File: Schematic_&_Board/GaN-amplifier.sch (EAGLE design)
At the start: 23 parts, among them T1 FDC3535, T2 NPN_MMBTA06FSCT, U1 TPS7A30XX, X1 SMA-142-0701-801/806, X2 SMA-142-0701-801/806

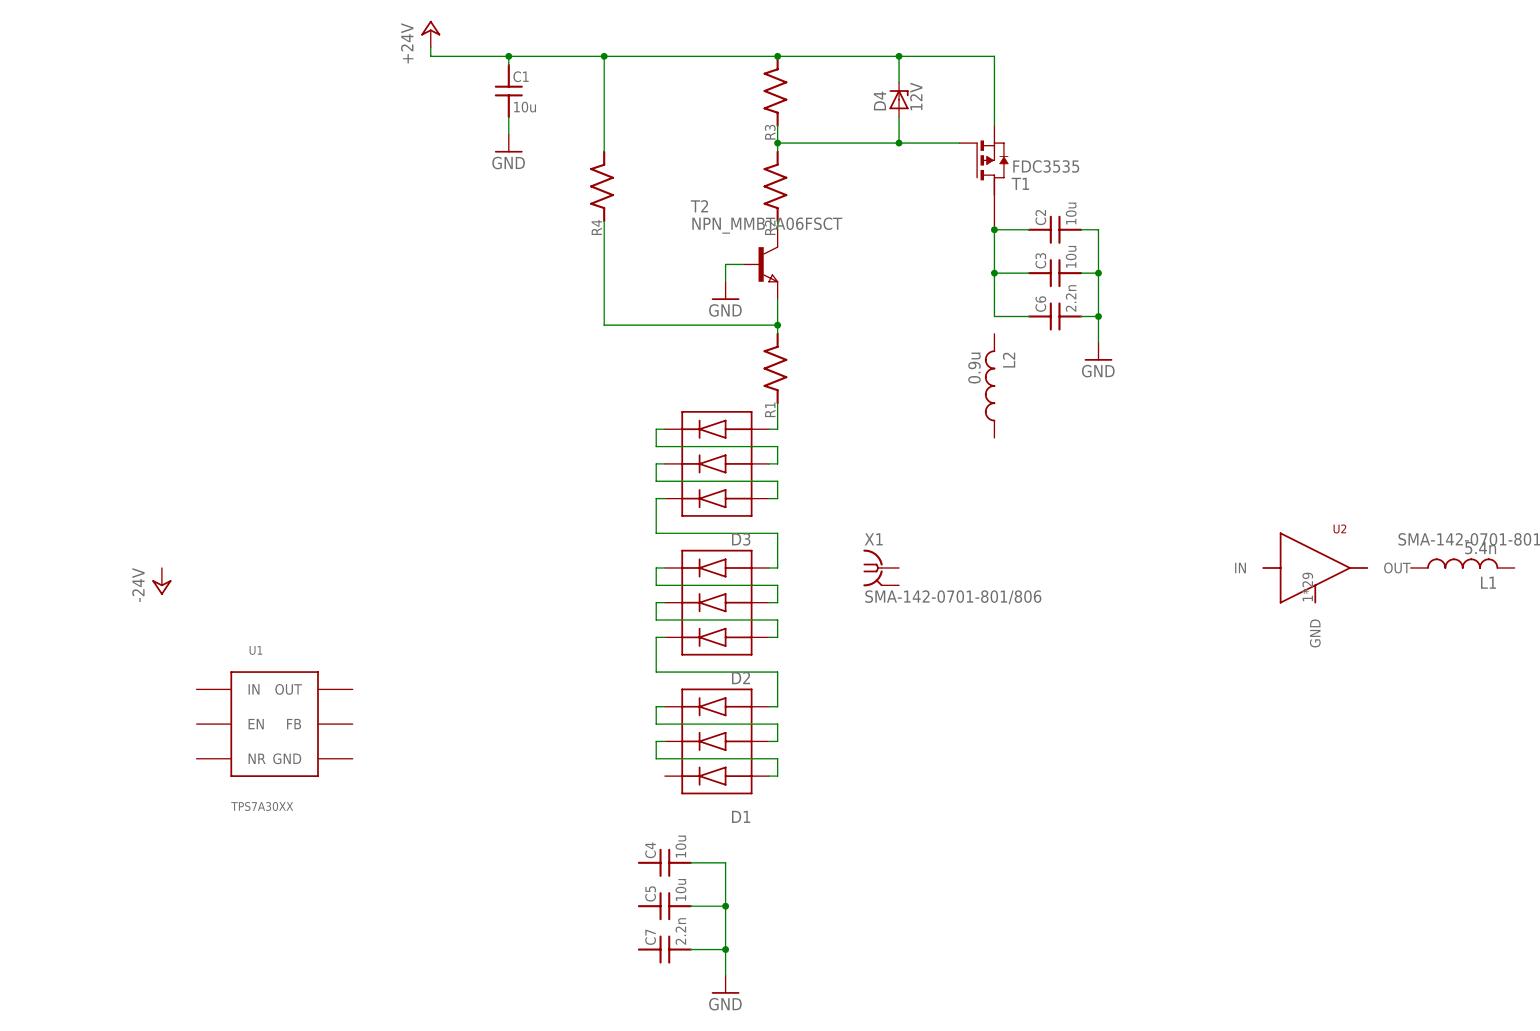
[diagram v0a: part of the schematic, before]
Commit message: Mostly designed power sequencing
This will all almost certainly be trashed, but it's a start.

DSB
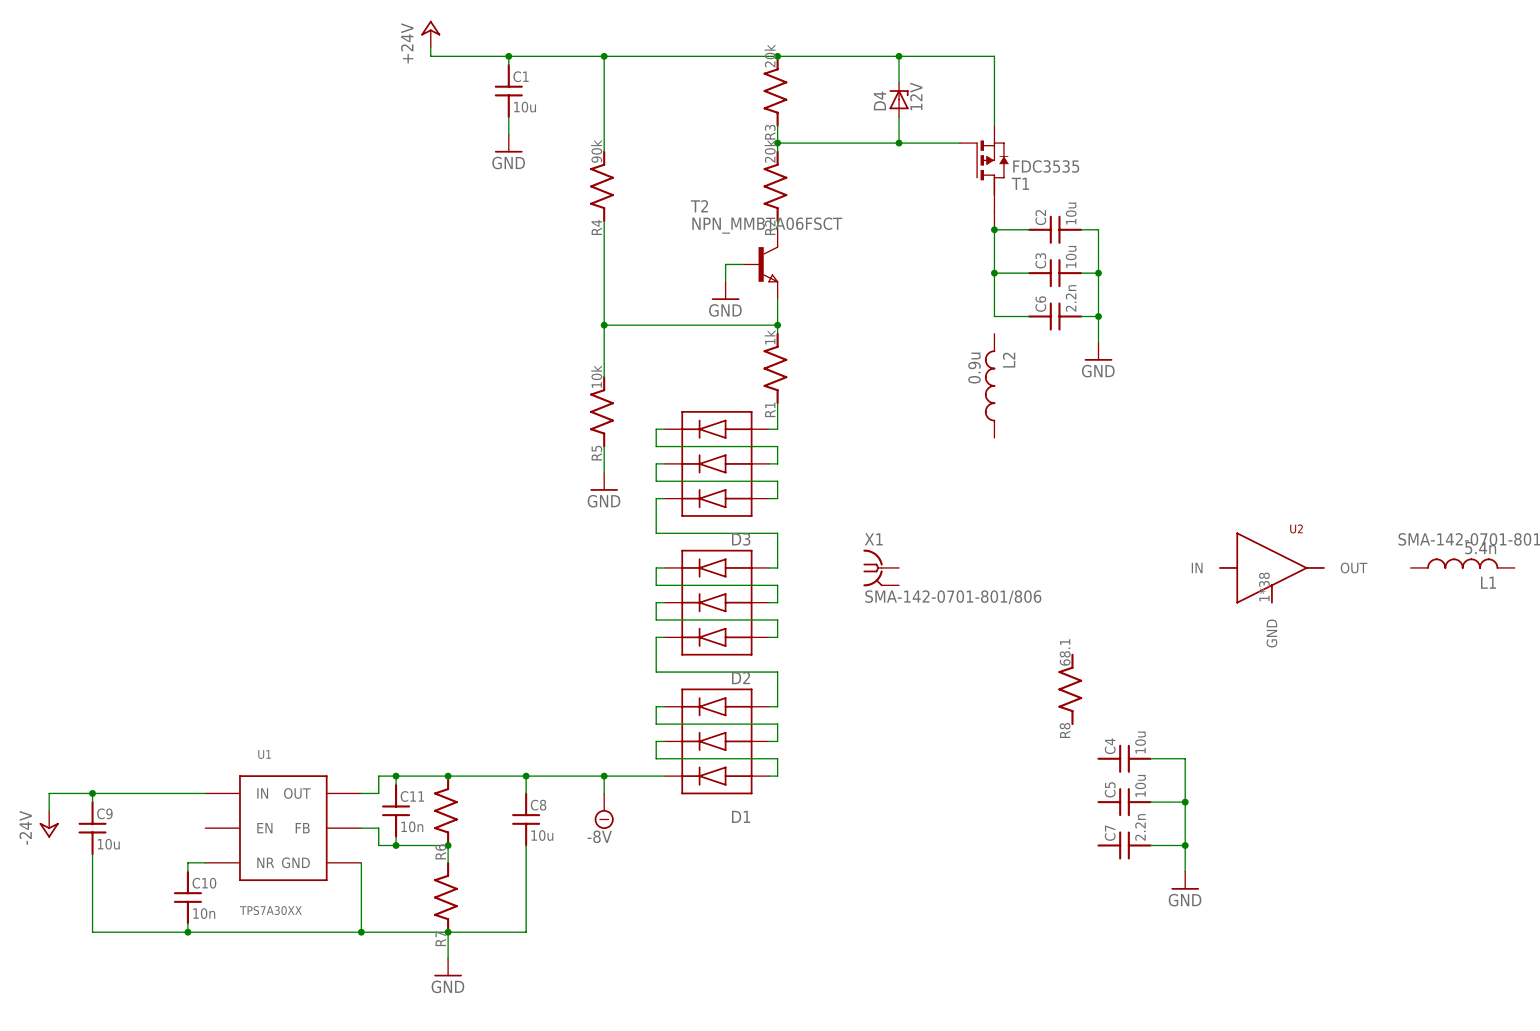
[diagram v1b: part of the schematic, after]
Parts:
- added C10, C11: 10n, jqi_passives:C_MLCC_SMDCMLCC_0402
- added C8, C9: 10u, jqi_passives:C_MLCC_SMDCMLCC_1206
- added R5: 10k, jqi_passives:R_SMDR0603
- added R6, R7: (no value), jqi_passives:R_SMDR0402
- added R8: 68.1, jqi_passives:R_SMDR0603
- R1: value (none) -> 1k
- R2, R3: value (none) -> 20k
- R4: value (none) -> 90k
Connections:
- new net -24V: C9.1, U1.IN
- new net -8V: C11.1, C8.1, D1.C1, R6.2, U1.OUT
- new net N$15: C11.2, R6.1, R7.2, U1.FB
- new net N$17: C10.1, U1.NR
- net GND: now also C10.2, C8.2, C9.2, R5.1, R7.1, U1.GND
- net N$3: now also R5.2
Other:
- moved on the sheet: C4, C5, C7, U1, U2

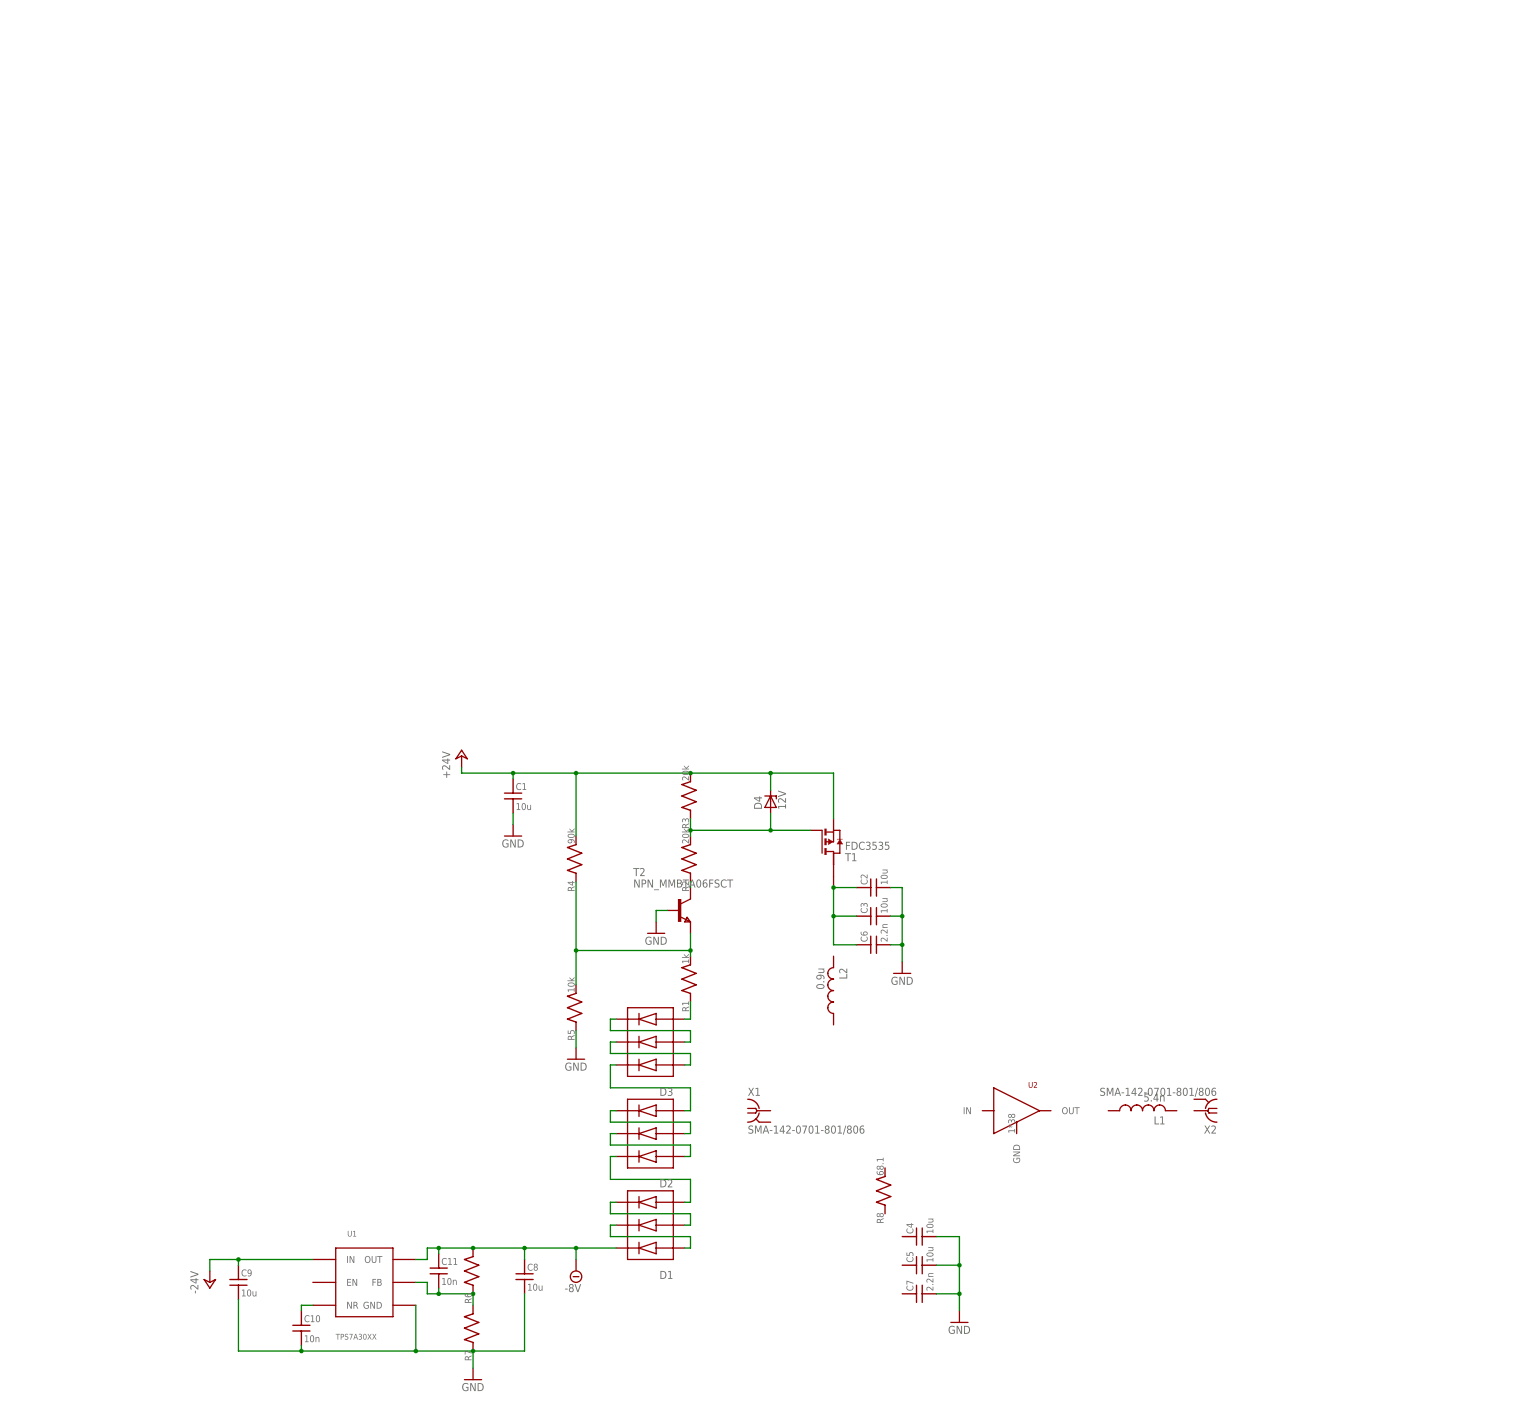
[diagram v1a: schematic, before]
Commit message: Change power sequencing
Switched to using LTC2924 for power sequencing.

DSB
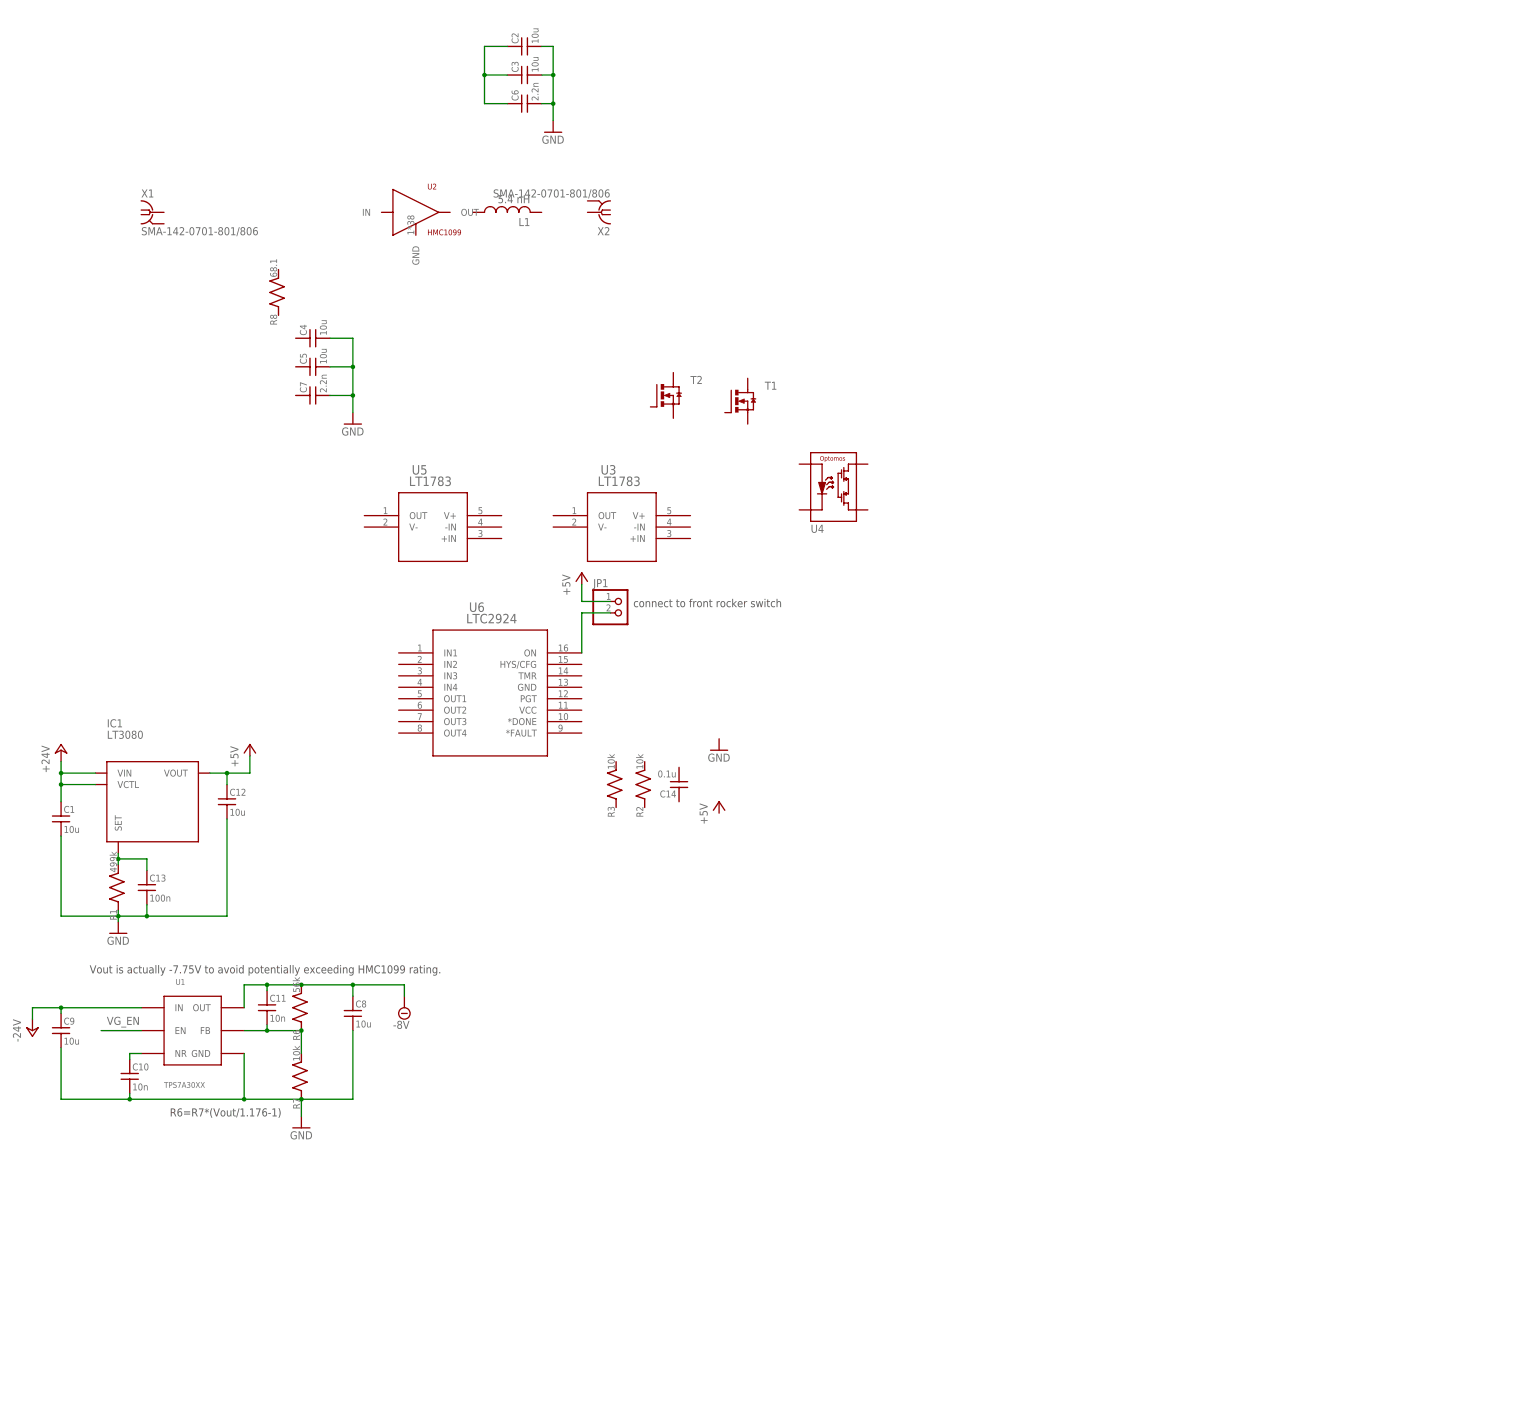
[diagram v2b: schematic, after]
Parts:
- removed D1, D2, D3: BAS16TW, qkdlab_alessandro:BAS16TW
- removed D4: 12V, qkdlab_alessandro:ZENER-DIODE
- removed L2: 0.9u, coilcraft-jqi:1008AF-XX
- removed R4: 90k, jqi_passives:R_SMDR0603
- removed R5: 10k, jqi_passives:R_SMDR0603
- added C12: 10u, jqi_passives:C_MLCC_SMDCMLCC_0805
- added C13: 100n, jqi_passives:C_MLCC_SMDCMLCC_0603
- added C14: 0.1u, jqi_passives:C_MLCC_SMDCMLCC_0603
- added IC1: LT3080, regulator-jqi:LT3080
- added JP1: (no value), pinhead:PINHD-1X2
- added U3, U5: LT1783, linear-technology-jqi:LT1783HS5
- added U4: CPC1117NTR, transistor-jqi:CPC1117NTR
- added U6: LTC2924, linear-technology-jqi:LTC2924IGN
- C1: device jqi_passives:C_MLCC_SMDCMLCC_1210 -> jqi_passives:C_MLCC_SMDCMLCC_0805
- L1: value 5.4n -> 5.4 nH
- R1: value 1k -> 499k
- R2, R3: value 20k -> 10k
- R6: value (none) -> 56k
- R7: value (none) -> 10k
- T1: value FDC3535 -> (none); device qkdlab_alessandro:PMOS-FDC3535SUPERSOT-6 -> transistor-jqi:IRL3714
- T2: value NPN_MMBTA06FSCT -> (none); device qkdlab_alessandro:NPN_MMBTA06FSCT -> transistor-jqi:IRL3714
- U2: value (none) -> HMC1099
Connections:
- removed net N$10: D2.A1, D2.C2
- removed net N$11: D1.A3, D2.C1
- removed net N$12: D1.A2, D1.C3
- removed net N$13: D1.A1, D1.C2
- removed net N$2: R2.1, T2.C
- removed net N$3: R1.2, R4.1, R5.2, T2.E
- removed net N$6: D3.A2, D3.C3
- removed net N$7: D3.A1, D3.C2
- removed net N$8: D2.A3, D3.C1
- removed net N$9: D2.A2, D2.C3
- new net +5V: C12.1, IC1.VOUT, JP1.1
- new net VG_EN: U1.EN
- net +24V: now also IC1.VCTL, IC1.VIN; no longer D4.C, R3.2, R4.2, T1.S
- net -8V: no longer D1.C1
- net GND: now also C12.2, C13.2, R1.1; no longer R5.1, T2.B
- net N$1: now also C13.1, IC1.SET, R1.2; no longer D4.A, R2.2, R3.1, T1.G
- net N$14: no longer T1.D3
- net N$4: now also JP1.2, U6.ON; no longer D3.A3, R1.1
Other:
- note added: "R6=R7*(Vout/1.176-1)"
- note added: "Vout is actually -7.75V to avoid potentially exceeding HMC1099 rating."
- note added: "connect to front rocker switch"
- moved on the sheet: C1, C10, C11, C2, C3, C4, C5, C6, C7, C8, C9, L1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

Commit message: Halfway done with power sequencing
The gate voltage supply and bias supply sequencing should be good to
go. Still need to set up the gate voltage and RF power lockout.

DSB
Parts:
- added C15: 150n, jqi_passives:C_MLCC_SMDCMLCC_0603
- added C16: 200n, jqi_passives:C_MLCC_SMDCMLCC_0603
- added C17, C18: 0.1u, jqi_passives:C_MLCC_SMDCMLCC_0603
- added Q1: MMBT3906LT1SMD, transistor-pnp:MMBT3906LT1SMD
- added R10: 10k, jqi_passives:R_SMDR0603
- added R11: 866, jqi_passives:R_SMDR0603
- added R12: 4.42k, jqi_passives:R_SMDR0603
- added R13: 1k, jqi_passives:R_SMDR0603
- added R14: 2M, jqi_passives:R_SMDR0603
- added R15: 54.9k, jqi_passives:R_SMDR0603
- added R4: 49.9k, jqi_passives:R_SMDR0603
- added R5: 1M, jqi_passives:R_SMDR0603
- added R9: 100k, jqi_passives:R_SMDR0603
- added T3: IRL3714S, transistor-jqi:IRL3714
- added U7: LCA701S, transistor-jqi:LCA701S
- T1, T2: value (none) -> IRL3714S
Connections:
- removed net N$14: C2.1, C3.1, C6.1
- removed net VG_EN: U1.EN
- new net AMP_POW: C11.1, C18.2, C8.1, R5.2, R6.2, T2.S, U1.OUT, U3.V-
- new net N$10: Q1.B, R9.2
- new net N$11: R13.2, T1.S
- new net N$12: R10.1, R11.1, U3.-IN
- new net N$13: R13.1, U7.C+
- new net N$2: R2.2, U6.*DONE
- new net N$3: R3.2, U6.*FAULT
- new net N$5: C16.1, U6.TMR
- new net N$6: R4.2, U6.HYS/CFG
- new net N$7: C15.1, U6.PGT
- new net N$8: R11.2, R12.1, U3.OUT
- new net N$9: Q1.C, R5.1, T2.G
- new net RF_DET: U6.IN4
- new net RF_EN: U6.OUT4
- new net VDD: C2.1, C3.1, C6.1, R14.1, U7.L-
- new net VDD_DET: R14.2, R15.2, U6.IN2
- new net VDD_EN: T1.G, U6.OUT2
- new net VGG_DET: U6.IN3
- new net VGG_EN: U6.OUT3
- new net VPIN_DET: R12.2, U6.IN1
- new net VPIN_EN: Q1.E, U6.OUT1
- net +24V: now also U7.L+
- net +5V: now also C14.1, C17.1, R2.1, R3.1, T1.D, U3.V+, U6.VCC
- net -24V: now also U1.EN
- net -8V: now also R10.2, T2.D; no longer C11.1, C8.1, R6.2, U1.OUT
- net GND: now also C14.2, C15.2, C16.2, C17.2, C18.1, R15.1, R4.1, R9.1, U3.+IN, U6.GND, U7.C-
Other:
- note added: "V(on,pinch)=0.61V*(R10/R11) V(off,pinch)=(0.61V-I_hys*R12)*(R10/R11) I_hys=10uA"
- moved on the sheet: C14, JP1, R2, R3, T1, T2, U3, U4, U5, U6
